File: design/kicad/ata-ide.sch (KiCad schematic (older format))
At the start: 29 parts, among them J1 Conn_02x32_Odd_Even, J2 Conn_02x20_Odd_Even, Q1 2N2907, U1 16V8, U2 ATF750, U3 74HCT241, U4 74HCT245, U5 74HCT245

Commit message: Update for version 1.1.
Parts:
- added C9: 4u7, Capacitors_THT:C_Rect_L7.0mm_W4.5mm_P5.00mm, symbol Device:C
- added J3: Conn_02x22_Odd_Even, Pin_Headers:Pin_Header_Straight_2x22_Pitch2.00mm, symbol Connector_Generic:Conn_02x22_Odd_Even
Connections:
- net +5V: now also C9.1, J3.41 (Pin_41), J3.42 (Pin_42)
- net A8: now also U1.18 (IO2); no longer U1.15 (IO5)
- net BA0: now also J3.35 (Pin_35)
- net BA1: now also J3.33 (Pin_33)
- net BA2: now also J3.36 (Pin_36)
- net BD0: now also J3.17 (Pin_17)
- net BD1: now also J3.15 (Pin_15)
- net BD10: now also J3.8 (Pin_8)
- net BD11: now also J3.10 (Pin_10)
- net BD12: now also J3.12 (Pin_12)
- net BD13: now also J3.14 (Pin_14)
- net BD14: now also J3.16 (Pin_16)
- net BD15: now also J3.18 (Pin_18)
- net BD2: now also J3.13 (Pin_13)
- net BD3: now also J3.11 (Pin_11)
- net BD4: now also J3.9 (Pin_9)
- net BD5: now also J3.7 (Pin_7)
- net BD6: now also J3.5 (Pin_5)
- net BD7: now also J3.3 (Pin_3)
- net BD8: now also J3.4 (Pin_4)
- net BD9: now also J3.6 (Pin_6)
- net CSEL: now also J3.28 (Pin_28)
- net DMACK: now also J3.29 (Pin_29)
- net GND: now also C9.2, J3.19 (Pin_19), J3.2 (Pin_2), J3.22 (Pin_22), J3.24 (Pin_24), J3.26 (Pin_26), J3.30 (Pin_30), J3.40 (Pin_40), J3.43 (Pin_43)
- net INTRQ: now also J3.31 (Pin_31)
- net ~BRESET~: now also J3.1 (Pin_1)
- net ~CS1~: now also J3.37 (Pin_37)
- net ~CS3~: now also J3.38 (Pin_38)
- net ~DASP~: now also J3.39 (Pin_39)
- net ~RD~: now also J3.25 (Pin_25)
- net ~WR~: now also J3.23 (Pin_23)
- net DMARQ: no longer names the net of J2.21 (Pin_21)
- no-connect marks 25 -> 31
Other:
- note added: "Only one of these two\nconnectors J2, J3 may\nbe fitted."
- note added: "Only place C9\nif 44-pin mini-\nconnector J3\nis selected."
- moved on the sheet: C1, C2, C3, C4, C5, C6, C7, C8, D1, J1, J2, JP1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

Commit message: PCB v1.1 RC1
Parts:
- removed JP3, JP4: SolderJumper_2_Open, Jumper:SolderJumper-2_P1.3mm_Open_Pad1.0x1.5mm, symbol Jumper:SolderJumper_2_Open
- added JP3, JP4: SolderJumper_2_Bridged, Jumper:SolderJumper-2_P1.3mm_Bridged_Pad1.0x1.5mm, symbol Jumper:SolderJumper_2_Bridged
- added R5: 10k, Resistors_THT:R_Axial_DIN0207_L6.3mm_D2.5mm_P10.16mm_Horizontal, symbol Device:R
- D1: Vendor uk.farnellcom 3218450 -> uk.farnell.com 2314284
- J3: Vendor (none) -> uk.farnell.com 1756945
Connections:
- net GND: now also R5.1
- net INTRQ: now also R5.2
- net ~IPL0~: now also JP3.2 (B)
- net ~IPL1~: now also JP4.2 (B)
- net at U3.7 (O1): now also JP4.1 (A)
- net at U3.9 (O0): now also JP3.1 (A)
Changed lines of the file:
@@
 	8100 5800 8100 5300
 Wire Wire Line
-	7100 4800 6200 4800
+	7100 4800 6000 4800
 Text GLabel 3500 4900 2    50   Input ~ 0
 R~W~
@@
 Wire Wire Line
 	8200 4800 7600 4800
-Text GLabel 7100 5400 0    50   Output ~ 0
+Text GLabel 6450 5550 0    50   Output ~ 0
 INTRQ
 $Comp
@@
 U 1 1 6026136B
 P 6650 5300
-F 0 "R1" V 6443 5300 50  0000 C CNN
-F 1 "10k" V 6534 5300 50  0000 C CNN
+F 0 "R1" V 6550 5250 50  0000 C CNN
+F 1 "10k" V 6550 5400 50  0000 C CNN
 F 2 "Resistors_THT:R_Axial_DIN0207_L6.3mm_D2.5mm_P10.16mm_Horizontal" V 6580 5300 50  0001 C CNN
 F 3 "~" H 6650 5300 50  0001 C CNN
@@
 L power:GND #PWR014
 U 1 1 603C6218
-P 6200 5350
-F 0 "#PWR014" H 6200 5100 50  0001 C CNN
-F 1 "GND" H 6205 5177 50  0000 C CNN
-F 2 "" H 6200 5350 50  0001 C CNN
-F 3 "" H 6200 5350 50  0001 C CNN
-	1    6200 5350
-	-1   0    0    -1
-$EndComp
-Wire Wire Line
-	6200 4800 6200 5350
+P 6000 5600
+F 0 "#PWR014" H 6000 5350 50  0001 C CNN
+F 1 "GND" H 6005 5427 50  0000 C CNN
+F 2 "" H 6000 5600 50  0001 C CNN
+F 3 "" H 6000 5600 50  0001 C CNN
+	1    6000 5600
+	-1   0    0    -1
+$EndComp
+Wire Wire Line
+	6000 4800 6000 5400
 Wire Wire Line
 	6900 2050 7250 2050
@@
 	650  6650 850  6650
 $Comp
-L Jumper:SolderJumper_2_Open JP3
-U 1 1 6064DE34
-P 9900 2600
-F 0 "JP3" H 9900 2805 50  0000 C CNN
-F 1 "SolderJumper_2_Open" H 10150 2700 50  0000 C CNN
-F 2 "Jumper:SolderJumper-2_P1.3mm_Open_Pad1.0x1.5mm" H 9900 2600 50  0001 C CNN
-F 3 "~" H 9900 2600 50  0001 C CNN
-	1    9900 2600
-	1    0    0    -1
-$EndComp
-$Comp
-L Jumper:SolderJumper_2_Open JP4
-U 1 1 6064FE61
-P 9900 2900
-F 0 "JP4" H 9900 3105 50  0000 C CNN
-F 1 "SolderJumper_2_Open" H 10150 3000 50  0000 C CNN
-F 2 "Jumper:SolderJumper-2_P1.3mm_Open_Pad1.0x1.5mm" H 9900 2900 50  0001 C CNN
-F 3 "~" H 9900 2900 50  0001 C CNN
-	1    9900 2900
-	1    0    0    -1
-$EndComp
-$Comp
 L Jumper:SolderJumper_2_Open JP5
 U 1 1 60650BAE
 P 9900 3200
-F 0 "JP5" H 9900 3405 50  0000 C CNN
+F 0 "JP5" H 10100 3150 50  0000 C CNN
 F 1 "SolderJumper_2_Open" H 10150 3300 50  0000 C CNN
 F 2 "Jumper:SolderJumper-2_P1.3mm_Open_Pad1.0x1.5mm" H 9900 3200 50  0001 C CNN
@@
 F 2 "LEDs:LED_D5.0mm" H 5250 6800 50  0001 C CNN
 F 3 "http://www.farnell.com/datasheets/1811043.pdf" H 5250 6800 50  0001 C CNN
-F 4 " uk.farnellcom 3218450" V 5250 6800 50  0001 C CNN "Vendor"
+F 4 " uk.farnell.com 2314284" V 5250 6800 50  0001 C CNN "Vendor"
 	1    5250 6800
 	0    1    -1   0
@@
 F 1 "Conn_02x22_Odd_Even" H 10200 3700 50  0000 C CNN
 F 2 "Pin_Headers:Pin_Header_Straight_2x22_Pitch2.00mm" H 10100 4900 50  0001 C CNN
-F 3 "~" H 10100 4900 50  0001 C CNN
+F 3 "http://www.farnell.com/datasheets/2701933.pdf" H 10100 4900 50  0001 C CNN
+F 4 "uk.farnell.com 1756945" H 10100 4900 50  0001 C CNN "Vendor"
 	1    10100 4900
 	1    0    0    -1
@@
 Only place C9\nif 44-pin mini-\nconnector J3\nis selected.
 NoConn ~ 4200 2050
+$Comp
+L Device:R R5
+U 1 1 6071BF2E
+P 6650 5400
+F 0 "R5" V 6750 5350 50  0000 C CNN
+F 1 "10k" V 6750 5500 50  0000 C CNN
+F 2 "Resistors_THT:R_Axial_DIN0207_L6.3mm_D2.5mm_P10.16mm_Horizontal" V 6580 5400 50  0001 C CNN
+F 3 "~" H 6650 5400 50  0001 C CNN
+	1    6650 5400
+	0    -1   1    0
+$EndComp
+Wire Wire Line
+	6800 5400 6850 5400
+Wire Wire Line
+	6500 5400 6000 5400
+Connection ~ 6000 5400
+Wire Wire Line
+	6000 5400 6000 5600
+Wire Wire Line
+	6850 5400 6850 5550
+Wire Wire Line
+	6850 5550 6450 5550
+Connection ~ 6850 5400
+Wire Wire Line
+	6850 5400 7100 5400
+$Comp
+L Jumper:SolderJumper_2_Bridged JP3
+U 1 1 6071DEF0
+P 9900 2600
+F 0 "JP3" H 10100 2550 50  0000 C CNN
+F 1 "SolderJumper_2_Bridged" H 10200 2700 50  0000 C CNN
+F 2 "Jumper:SolderJumper-2_P1.3mm_Bridged_Pad1.0x1.5mm" H 9900 2600 50  0001 C CNN
+F 3 "~" H 9900 2600 50  0001 C CNN
+	1    9900 2600
+	1    0    0    -1
+$EndComp
+$Comp
+L Jumper:SolderJumper_2_Bridged JP4
+U 1 1 60724169
+P 9900 2900
+F 0 "JP4" H 10100 2850 50  0000 C CNN
+F 1 "SolderJumper_2_Bridged" H 10200 3000 50  0000 C CNN
+F 2 "Jumper:SolderJumper-2_P1.3mm_Bridged_Pad1.0x1.5mm" H 9900 2900 50  0001 C CNN
+F 3 "~" H 9900 2900 50  0001 C CNN
+	1    9900 2900
+	1    0    0    -1
+$EndComp
 $EndSCHEMATC

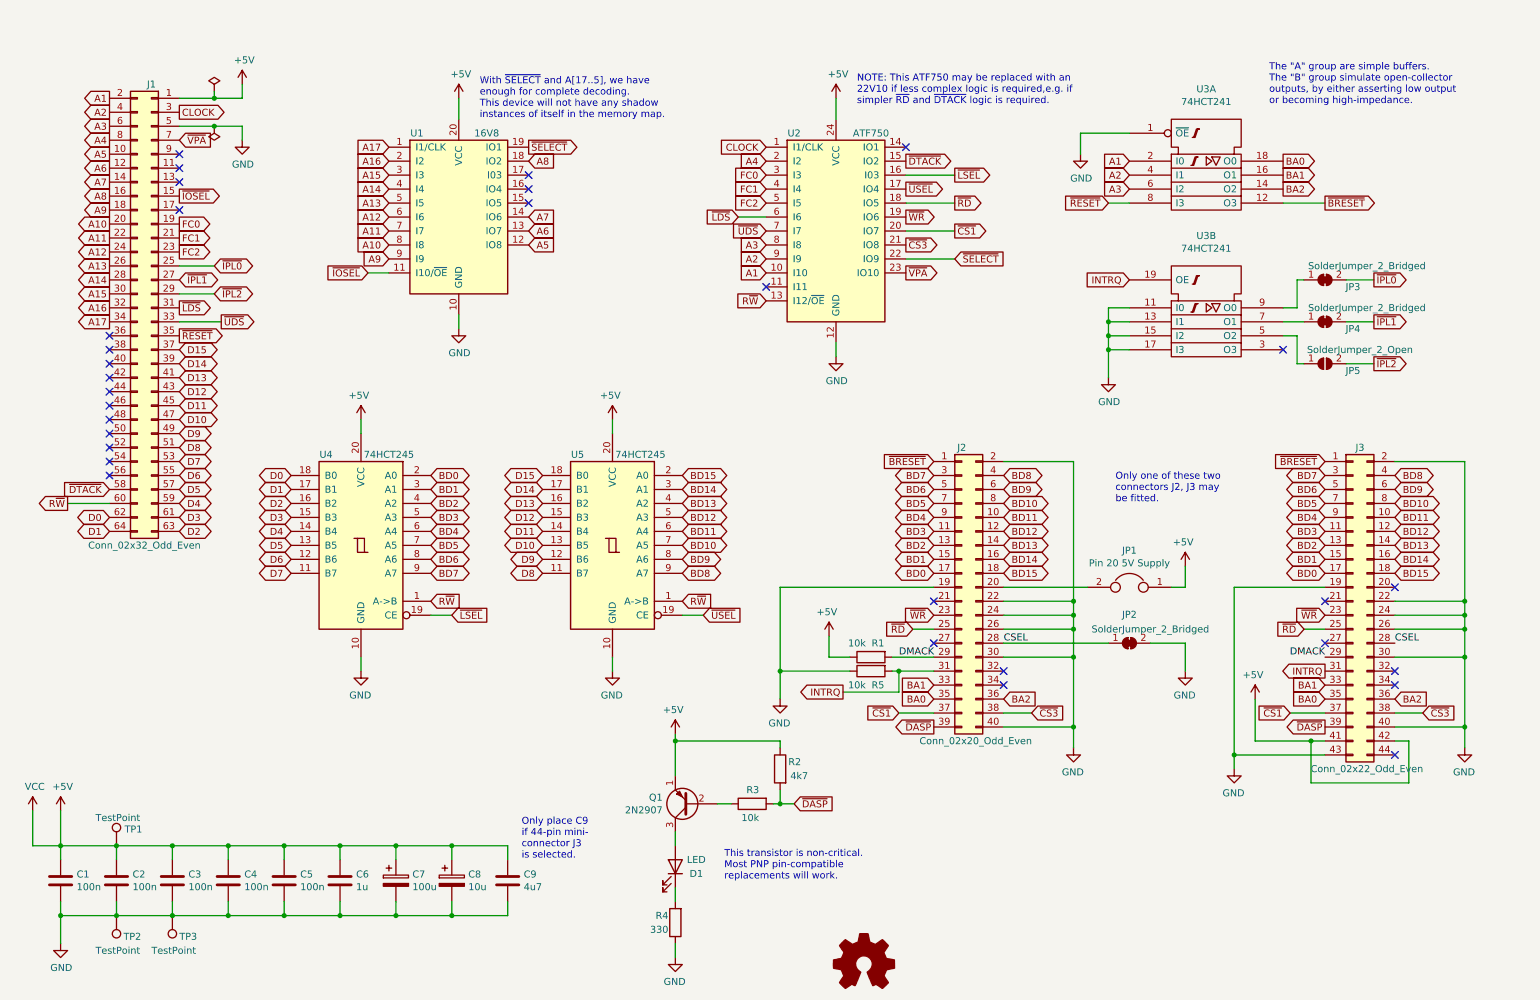
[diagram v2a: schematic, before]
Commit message: Add some tweeks to make things easier for builders.
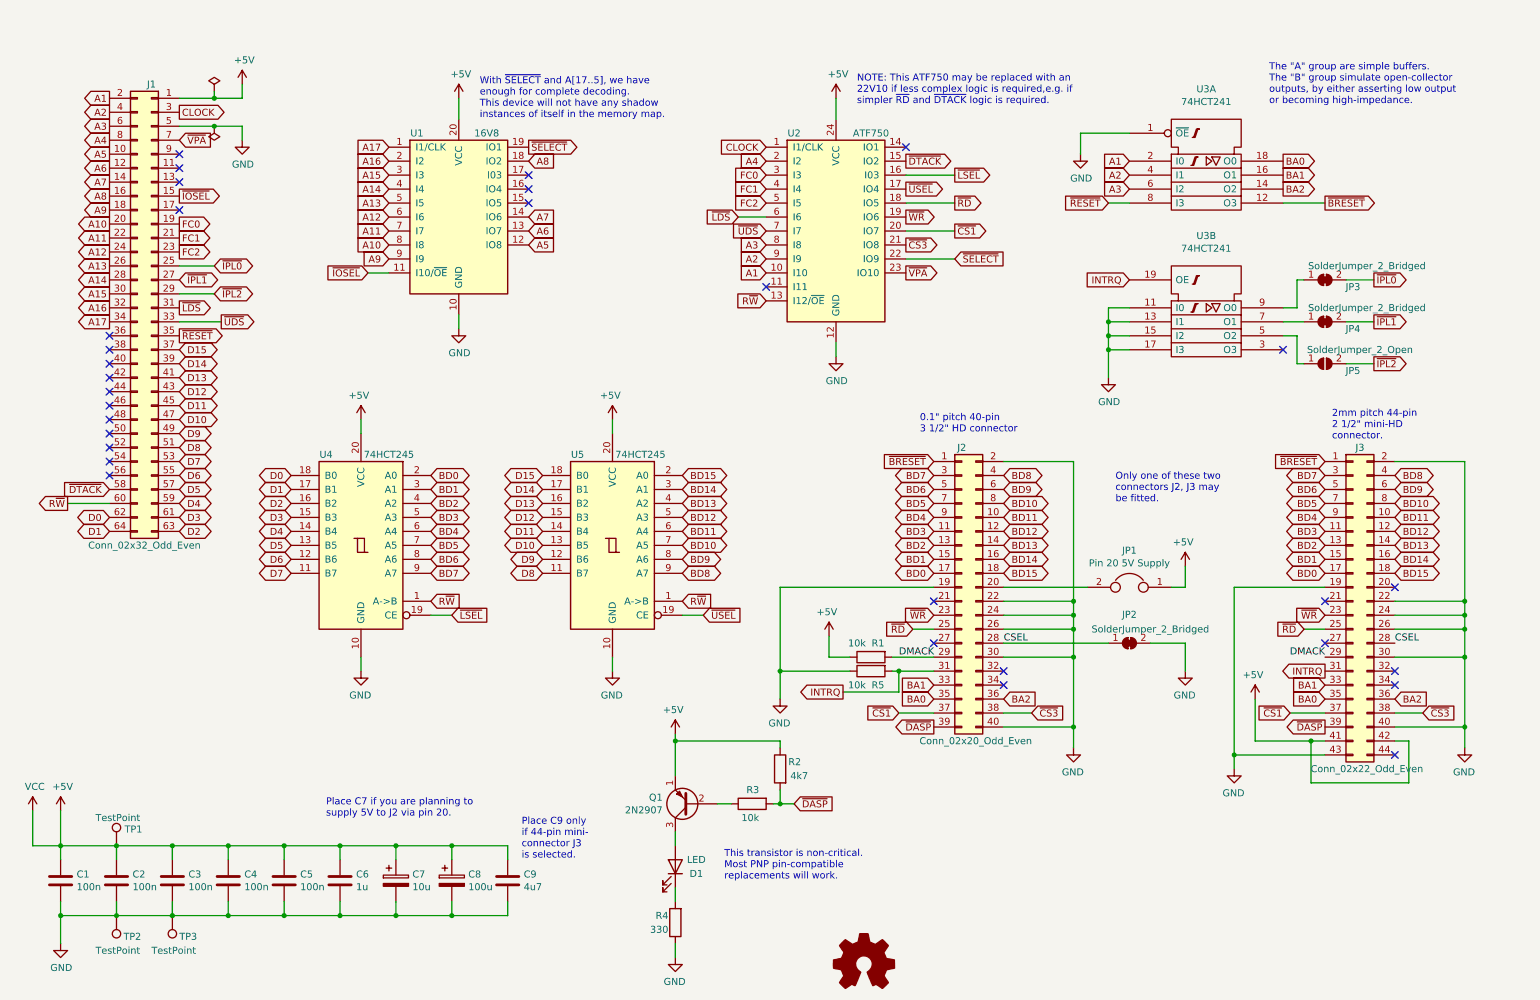
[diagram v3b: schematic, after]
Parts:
- C7: value 100u -> 10u
- C8: value 10u -> 100u
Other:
- note added: "0.1" pitch 40-pin\n3 1/2" HD connector"
- note added: "2mm pitch 44-pin\n2 1/2" mini-HD\nconnector."
- note added: "Place C7 if you are planning to\nsupply 5V to J2 via pin 20."
- note added: "Place C9 only\nif 44-pin mini-\nconnector J3\nis selected."
- note removed: "Only place C9\nif 44-pin mini-\nconnector J3\nis selected."
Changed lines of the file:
@@
 P 3250 6900
 F 0 "C7" H 3368 6946 50  0000 L CNN
-F 1 "100u" H 3368 6855 50  0000 L CNN
+F 1 "10u" H 3368 6855 50  0000 L CNN
 F 2 "Capacitors_THT:CP_Radial_D8.0mm_P2.50mm" H 3288 6750 50  0001 C CNN
 F 3 "~" H 3250 6900 50  0001 C CNN
@@
 P 3650 6900
 F 0 "C8" H 3768 6946 50  0000 L CNN
-F 1 "10u" H 3768 6855 50  0000 L CNN
+F 1 "100u" H 3768 6855 50  0000 L CNN
 F 2 "Capacitors_THT:CP_Radial_D8.0mm_P2.50mm" H 3688 6750 50  0001 C CNN
 F 3 "~" H 3650 6900 50  0001 C CNN
@@
 Connection ~ 3650 7150
 Text Notes 4150 6750 0    50   ~ 0
-Only place C9\nif 44-pin mini-\nconnector J3\nis selected.
+Place C9 only\nif 44-pin mini-\nconnector J3\nis selected.
 NoConn ~ 4200 2050
 $Comp
@@
 	1    0    0    -1
 $EndComp
+Text Notes 2750 6450 0    50   ~ 0
+Place C7 if you are planning to\nsupply 5V to J2 via pin 20.
+Text Notes 7000 3700 0    50   ~ 0
+0.1" pitch 40-pin\n3 1/2" HD connector
+Text Notes 9950 3750 0    50   ~ 0
+2mm pitch 44-pin\n2 1/2" mini-HD\nconnector.
 $EndSCHEMATC
